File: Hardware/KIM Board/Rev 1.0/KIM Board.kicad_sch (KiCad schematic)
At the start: 112 parts, among them J1 KIM ENABLE, J2 DB9 FEMALE (DCE), J3 CTS EN, J4 CARD SLOT, J5 6502 BUS, J6 BREADBOARD HEADERS, J7 5V DC, Q1 2N3904, SW1 0, SW10 9, SW11 10, SW12 11, SW13 12, SW14 13, SW15 14, SW16 15, SW17 16, SW18 17, SW19 18, SW2 1, SW20 19, SW21 20, SW22 21, SW23 22, SW24 23, SW25 IO ENABLE, SW26 RESET, SW27 POWER, SW3 2, SW4 3, SW5 4, SW6 5, SW7 6, SW8 7, SW9 8, U1 65C02, U10 74HC138, U11 74HC138, U12 LM555, U13 LCD-16X2, U14 MAX232, U15 R6551AP, U16 MM74C922, U17 74HC00, U2 AS6C62256, U3 AT28C256, U4 74HC00, U5 74HC00, U6 74HC00, U7 74HC138, U8 W65C21N, U9 AT28C64, X1 1 MHz, Y1 1.8432 Mhz

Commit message: KIM Board Rev 1.0: J4 is CART and J5 is BUS
The card slot's and the 6502 BUS header's value fields now read CART
and BUS, as on the ACE, where they were CARD SLOT and 6502 BUS. The
schematic PDF is plotted again, and check-schematics.mjs looks for the
new values, and passes.

Co-Authored-By: Claude Opus 5.5 <noreply@anthropic.com>
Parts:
- J4: value CARD SLOT -> CART
- J5: value 6502 BUS -> BUS
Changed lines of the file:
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@@
 			)
 		)
-		(property "Value" "6502 BUS"
+		(property "Value" "BUS"
 			(at 506.73 287.782 0)
 			(show_name no)
@@
 			)
 		)
-		(property "Value" "CARD SLOT"
+		(property "Value" "CART"
 			(at 461.01 287.782 0)
 			(show_name no)

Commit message: KIM Board Rev 1.0: pull the PIA's CB1 and CB2 up through R23
CB1 and CB2 are unused, and as CMOS inputs they floated. They are now
joined and held high by one 10k (R23), placed under the LCD. A resistor
rather than a tie to VCC, because software can make CB2 an output.

- Schematic: R23 replaces the two no-connects; the PDF is re-exported.
- PCB: R23 placed, with R15's order fields; the GND pours refilled.
- Tests/check-schematics.mjs checks that CB1 and CB2 are joined and
  have one 10k pull-up.
- README: R23 in the keypad and display bullet, and in the checks.

Co-Authored-By: Claude Opus 5.5 <noreply@anthropic.com>
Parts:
- added R23: 10k, Resistor_THT:R_Axial_DIN0204_L3.6mm_D1.6mm_P5.08mm_Horizontal, symbol Device:R
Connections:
- net VCC: now also R23.1
- net at U8.18 (CB1): now also U8.19 (CB2), R23.2
- no-connect marks 29 -> 27
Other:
- moved on the sheet: C13, C14, C15, C16, C17, C18, C19, C20, C21, C22, C23, C24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

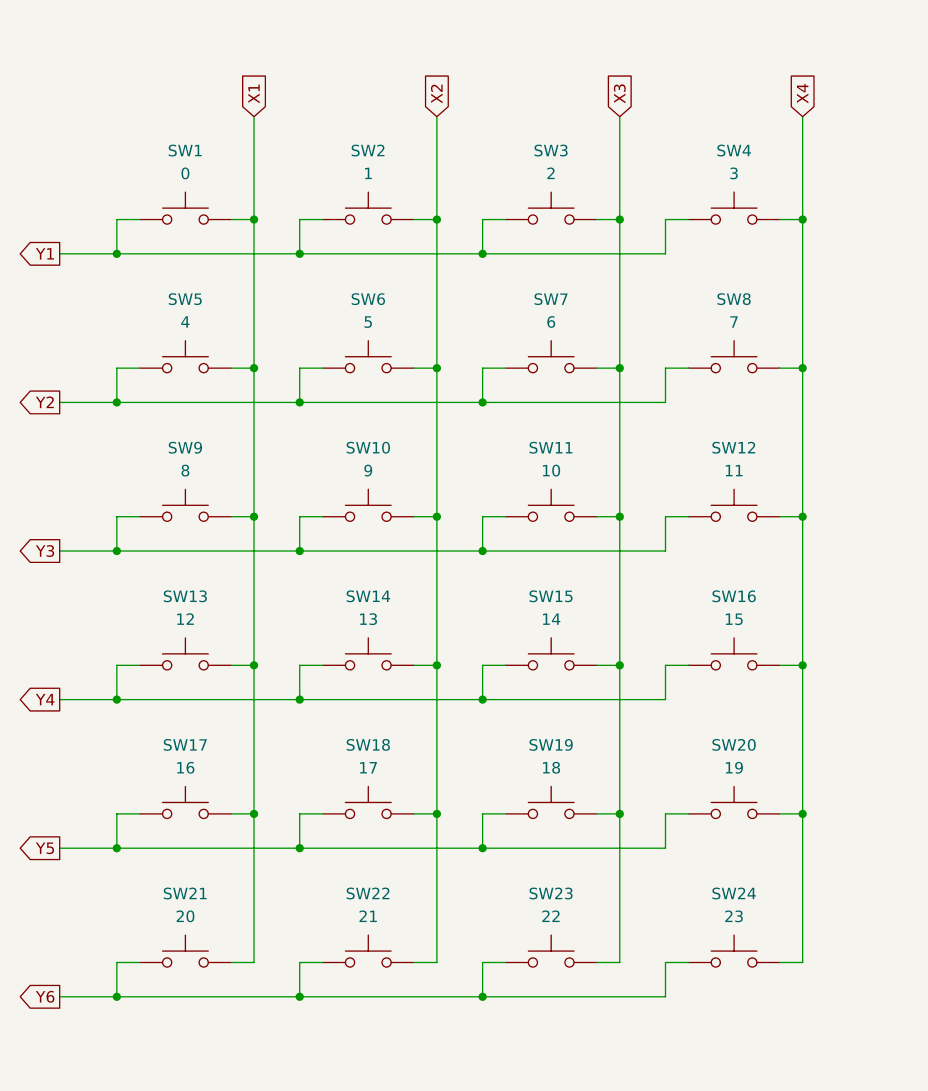
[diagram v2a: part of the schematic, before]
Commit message: KIM Board Rev 1.0: label the keypad switches with their KIM keys
The 24 matrix switches carried their keycodes (0-23) as values, which
only matched the key for 1-9. Each now carries the key the KC Monitor
gives that keycode (kim.inc): SW1 LEFT, SW11 0, SW12 RIGHT, SW13-SW16
F E D C, SW17 ESC, SW18 INS, SW19 PGUP, SW20 A, SW21 UP, SW22 DEL,
SW23 PGDN, SW24 B.

- Schematic and PCB: the values changed, nothing else; schematic
  parity is clean.
- The schematic PDF is re-exported.

Co-Authored-By: Claude Opus 5.5 <noreply@anthropic.com>
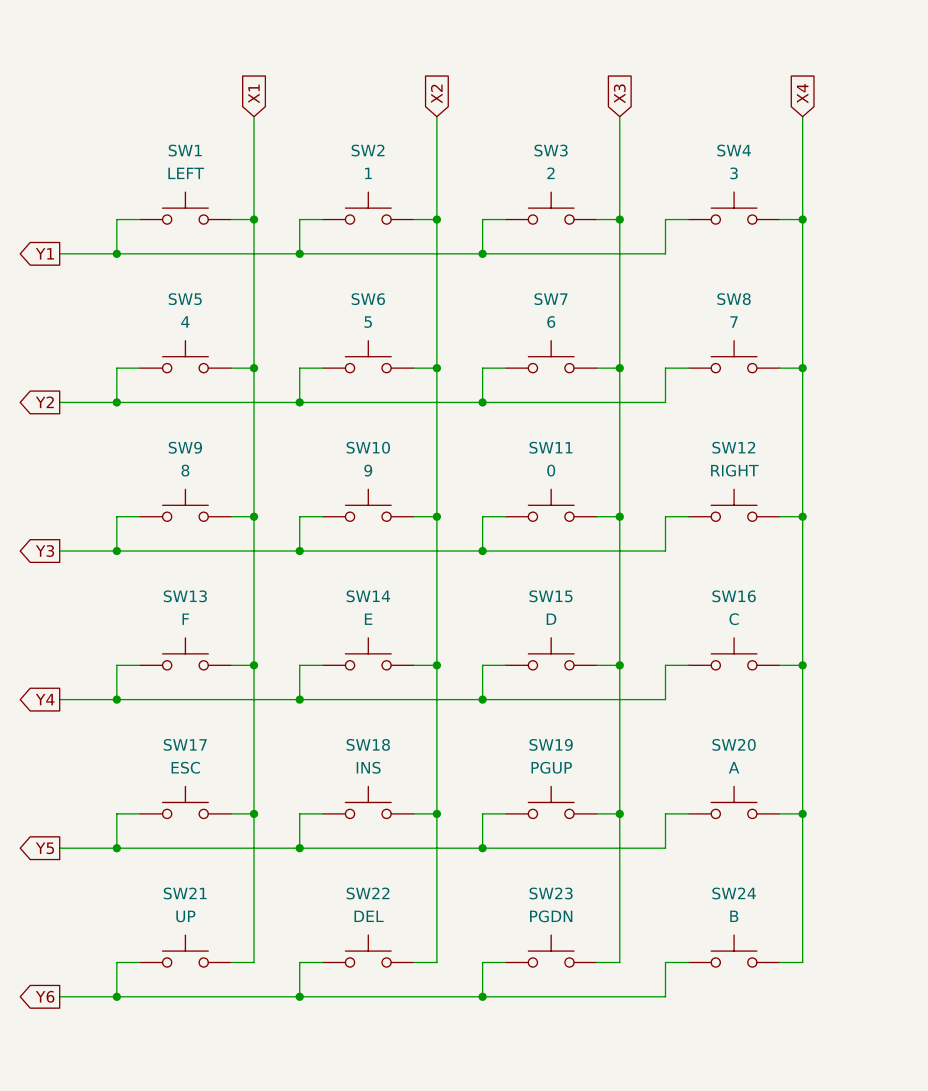
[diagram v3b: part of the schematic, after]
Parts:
- SW1: value 0 -> LEFT
- SW11: value 10 -> 0
- SW12: value 11 -> RIGHT
- SW13: value 12 -> F
- SW14: value 13 -> E
- SW15: value 14 -> D
- SW16: value 15 -> C
- SW17: value 16 -> ESC
- SW18: value 17 -> INS
- SW19: value 18 -> PGUP
- SW20: value 19 -> A
- SW21: value 20 -> UP
- SW22: value 21 -> DEL
- SW23: value 22 -> PGDN
- SW24: value 23 -> B
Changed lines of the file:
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@@
 			)
 		)
-		(property "Value" "14"
+		(property "Value" "D"
 			(at 656.59 92.71 0)
 			(show_name no)
@@
 			)
 		)
-		(property "Value" "16"
+		(property "Value" "ESC"
 			(at 615.95 109.22 0)
 			(show_name no)
@@
 			)
 		)
-		(property "Value" "12"
+		(property "Value" "F"
 			(at 615.95 92.71 0)
 			(show_name no)
@@
 			)
 		)
-		(property "Value" "23"
+		(property "Value" "B"
 			(at 676.91 125.73 0)
 			(show_name no)
@@
 			)
 		)
-		(property "Value" "21"
+		(property "Value" "DEL"
 			(at 636.27 125.73 0)
 			(show_name no)
@@
 			)
 		)
-		(property "Value" "20"
+		(property "Value" "UP"
 			(at 615.95 125.73 0)
 			(show_name no)
@@
 			)
 		)
-		(property "Value" "17"
+		(property "Value" "INS"
 			(at 636.27 109.22 0)
 			(show_name no)
@@
 			)
 		)
-		(property "Value" "10"
+		(property "Value" "0"
 			(at 656.59 76.2 0)
 			(show_name no)
@@
 			)
 		)
-		(property "Value" "19"
+		(property "Value" "A"
 			(at 676.91 109.22 0)
 			(show_name no)
@@
 			)
 		)
-		(property "Value" "18"
+		(property "Value" "PGUP"
 			(at 656.59 109.22 0)
 			(show_name no)
@@
 			)
 		)
-		(property "Value" "22"
+		(property "Value" "PGDN"
 			(at 656.59 125.73 0)
 			(show_name no)
@@
 			)
 		)
-		(property "Value" "15"
+		(property "Value" "C"
 			(at 676.91 92.71 0)
 			(show_name no)
@@
 			)
 		)
-		(property "Value" "11"
+		(property "Value" "RIGHT"
 			(at 676.91 76.2 0)
 			(show_name no)
@@
 			)
 		)
-		(property "Value" "13"
+		(property "Value" "E"
 			(at 636.27 92.71 0)
 			(show_name no)
@@
 			)
 		)
-		(property "Value" "0"
+		(property "Value" "LEFT"
 			(at 615.95 43.18 0)
 			(show_name no)

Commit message: KIM Board Rev 1.0: arrows for the keypad's LEFT, RIGHT and UP keys
SW1, SW12 and SW21 now carry ←, → and ↑ in place of LEFT, RIGHT and
UP, on the schematic and the PCB's silkscreen. KiCad's stroke font
draws all three. Schematic parity is clean, and the schematic PDF is
re-exported.

Co-Authored-By: Claude Opus 5.5 <noreply@anthropic.com>
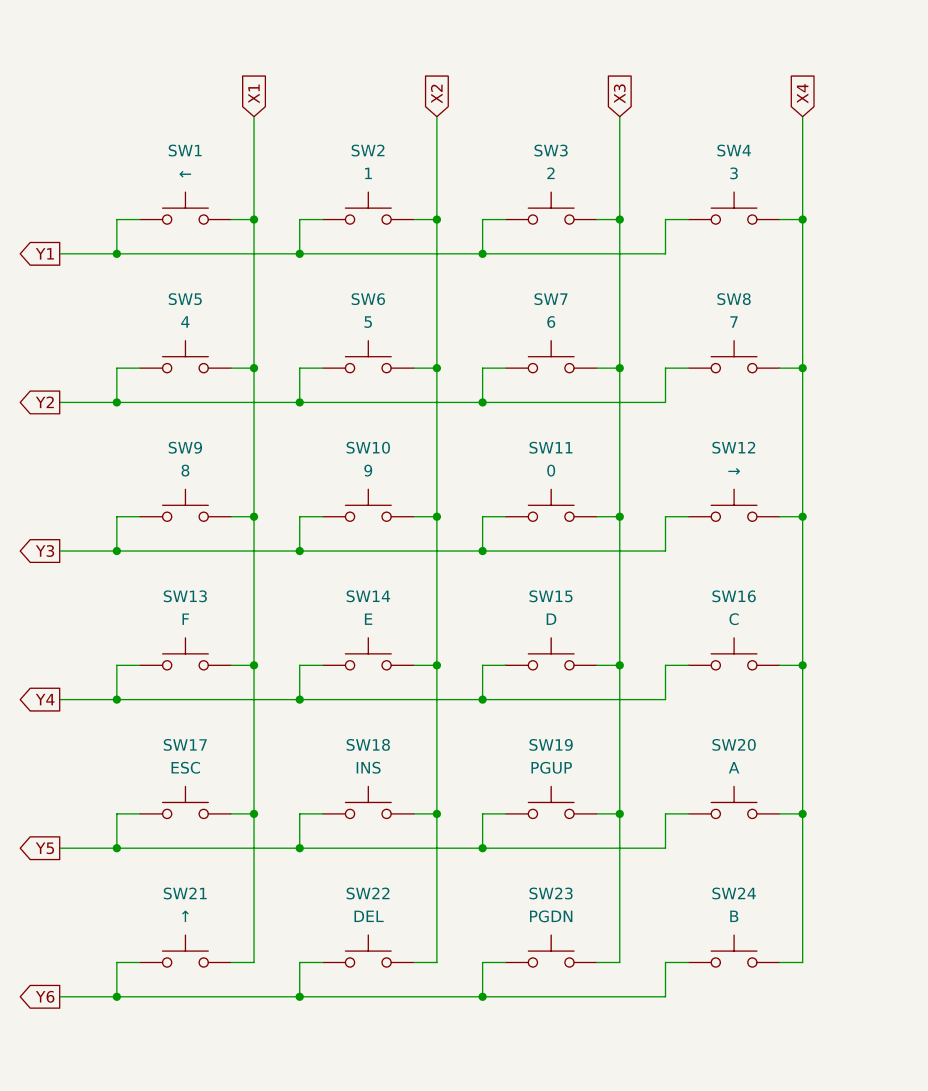
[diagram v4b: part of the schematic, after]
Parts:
- SW1: value LEFT -> ←
- SW12: value RIGHT -> →
- SW21: value UP -> ↑
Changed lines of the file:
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@@
 			)
 		)
-		(property "Value" "UP"
+		(property "Value" "↑"
 			(at 615.95 125.73 0)
 			(show_name no)
@@
 			)
 		)
-		(property "Value" "RIGHT"
+		(property "Value" "→"
 			(at 676.91 76.2 0)
 			(show_name no)
@@
 			)
 		)
-		(property "Value" "LEFT"
+		(property "Value" "←"
 			(at 615.95 43.18 0)
 			(show_name no)

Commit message: KIM Board Rev 1.0: words again for the keypad's LEFT, RIGHT and UP keys
This reverts commit 416ed65. The owner prefers the words to the arrows,
so SW1, SW12 and SW21 carry LEFT, RIGHT and UP again, as the KC Monitor
names them. The schematic PDF goes back with them.

Co-Authored-By: Claude Opus 5.5 <noreply@anthropic.com>
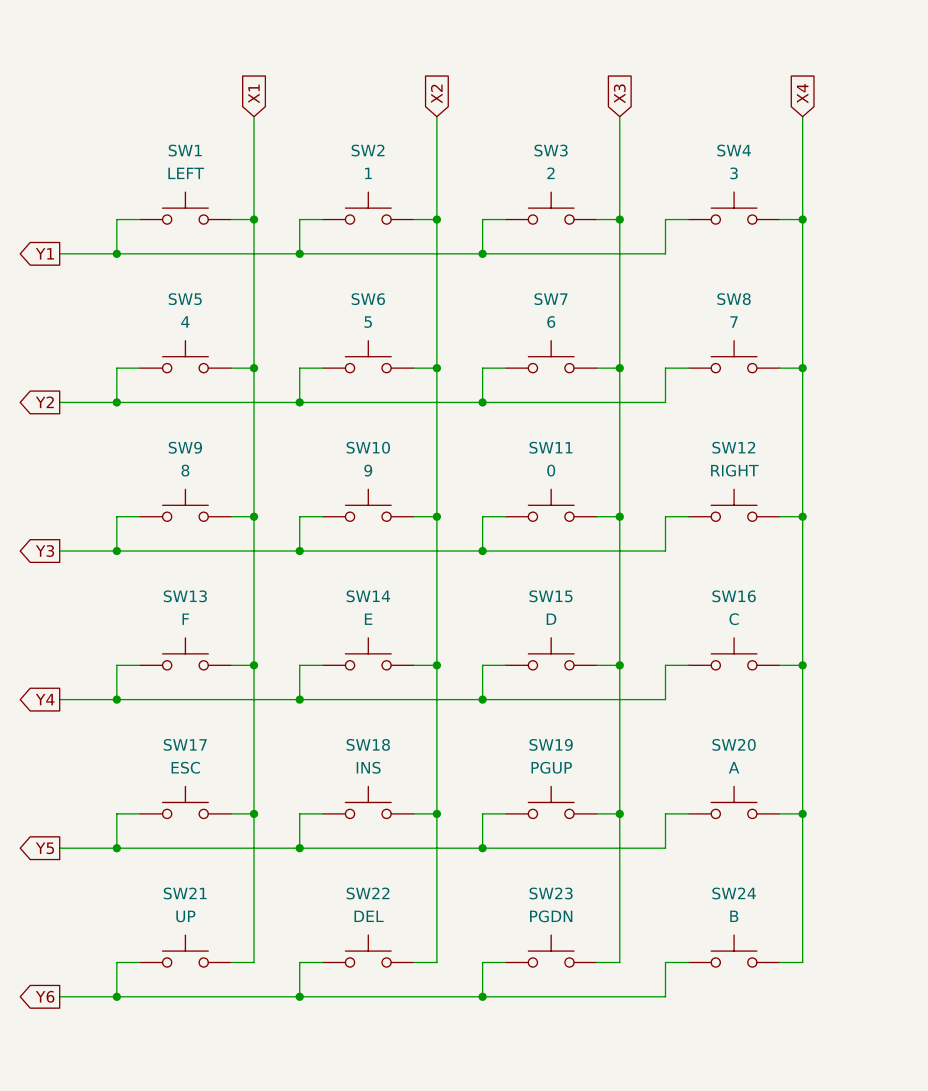
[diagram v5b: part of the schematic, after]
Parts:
- SW1: value ← -> LEFT
- SW12: value → -> RIGHT
- SW21: value ↑ -> UP
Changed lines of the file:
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@@
 			)
 		)
-		(property "Value" "↑"
+		(property "Value" "UP"
 			(at 615.95 125.73 0)
 			(show_name no)
@@
 			)
 		)
-		(property "Value" "→"
+		(property "Value" "RIGHT"
 			(at 676.91 76.2 0)
 			(show_name no)
@@
 			)
 		)
-		(property "Value" "←"
+		(property "Value" "LEFT"
 			(at 615.95 43.18 0)
 			(show_name no)
